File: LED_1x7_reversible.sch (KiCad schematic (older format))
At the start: 14 parts

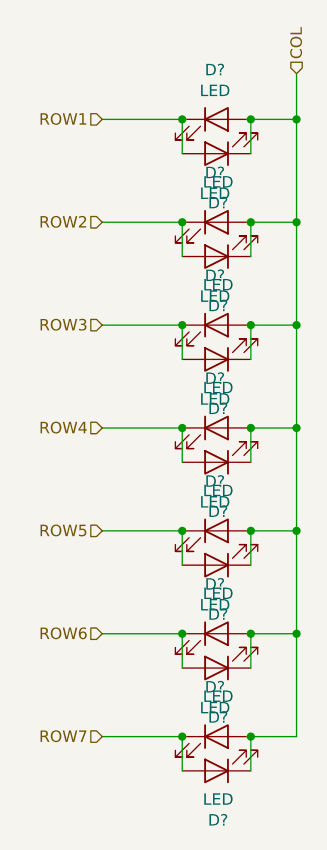
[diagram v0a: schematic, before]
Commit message: Placed 14x9 grid
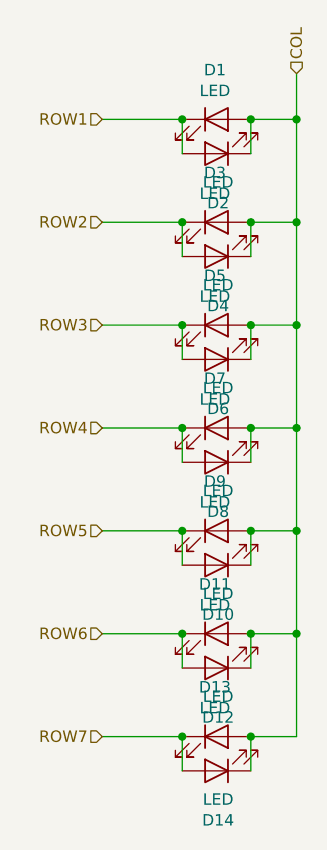
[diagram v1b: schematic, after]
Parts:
- D1, D10, D11, D12, D13, D14, D2, D3, D4, D5, D6, D7, D8, D9: renamed from D?; footprint (none) -> LED_SMD:LED_0805_2012Metric

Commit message: Fix matrix
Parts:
- removed D8: LED, LED_SMD:LED_0805_2012Metric, symbol Device:LED
- added D2: LED, LED_SMD:LED_0805_2012Metric, symbol Device:LED
- renumbered D2 to D8
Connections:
- net COL: now also D1.1 (K), D10.2 (A), D12.2 (A), D14.2 (A), D3.1 (K), D5.1 (K), D7.1 (K), D8.2 (A), D2.1 (K); no longer D1.2 (A), D10.1 (K), D12.1 (K), D14.1 (K), D3.2 (A), D5.2 (A), D7.2 (A), D8.1 (K)
- net ROW1: now also D1.2 (A), D8.1 (K); no longer D1.1 (K), D8.2 (A)
- net ROW2: now also D9.1 (K), D2.2 (A); no longer D3.1 (K), D4.2 (A)
- net ROW3: now also D10.1 (K), D3.2 (A); no longer D5.1 (K), D6.2 (A)
- net ROW4: now also D11.1 (K), D4.2 (A); no longer D7.1 (K)
- net ROW5: now also D12.1 (K), D5.2 (A); no longer D10.2 (A), D9.1 (K)
- net ROW6: now also D13.1 (K), D6.2 (A); no longer D11.1 (K), D12.2 (A)
- net ROW7: now also D14.1 (K), D7.2 (A); no longer D13.1 (K), D14.2 (A)
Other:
- moved on the sheet: D113, D120
